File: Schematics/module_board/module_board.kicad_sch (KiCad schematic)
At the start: 38 parts, among them J1 Conn_01x01_Male, J2 Conn_01x06_Male, J3 Conn_01x06_Male, SW1 SW_SPST, SW2 SW_Push, SW3 SW_Push, SW4 SW_Push, SW5 SW_Push, SW6 SW_Push, U1 RP2040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

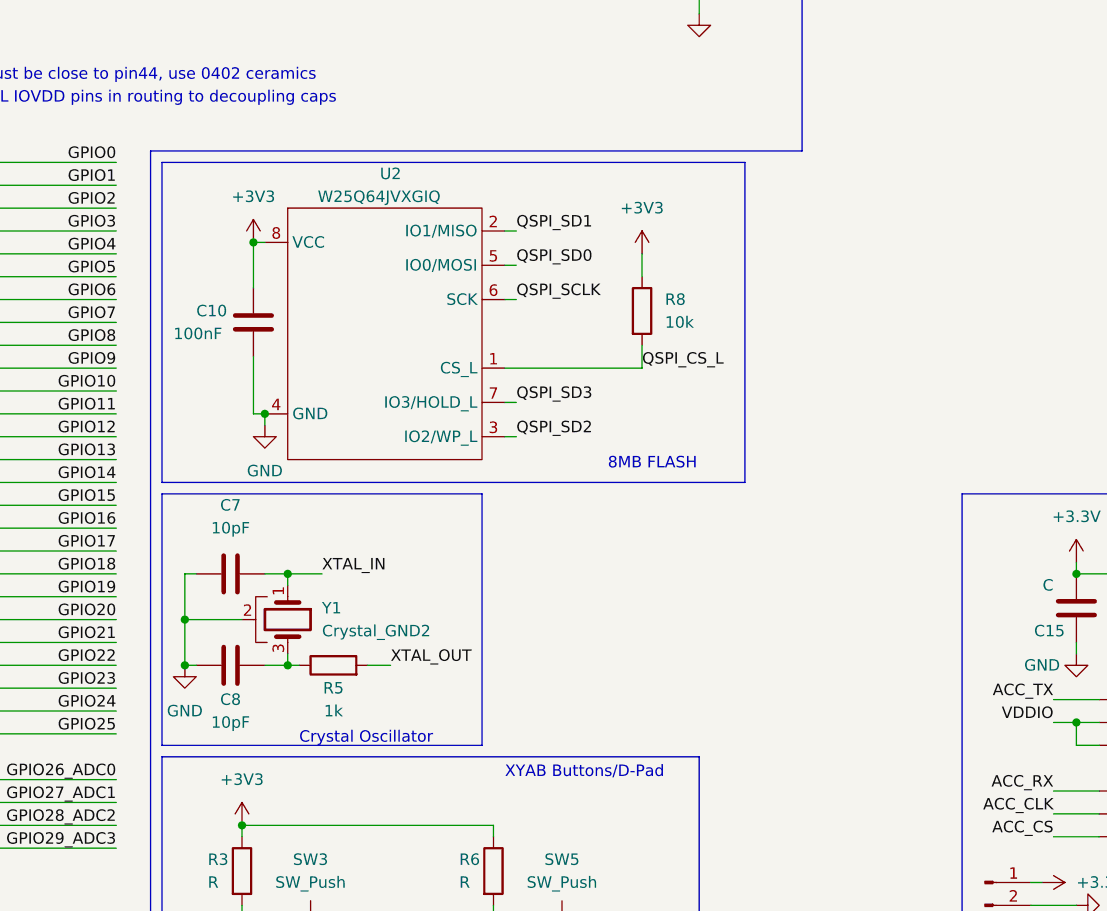
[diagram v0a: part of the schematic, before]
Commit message: updated crystal oscillator and flash memory on module board
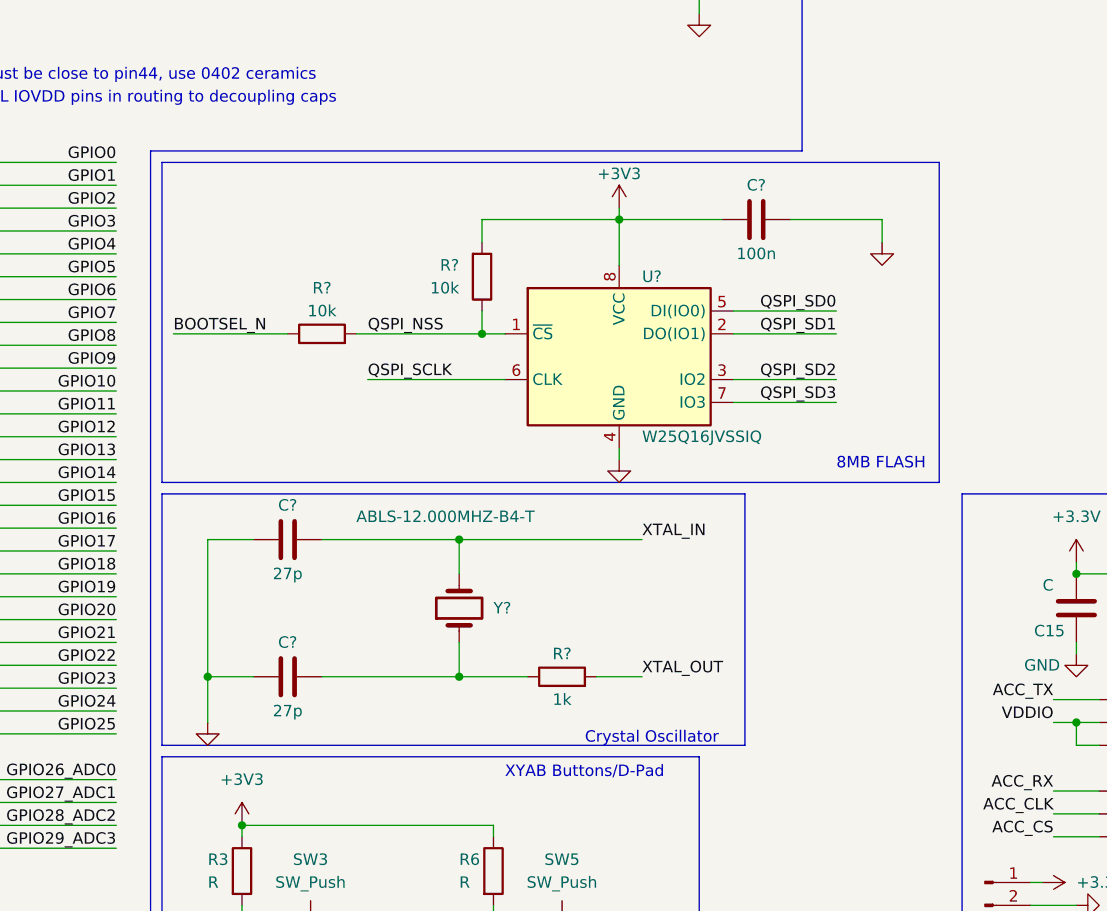
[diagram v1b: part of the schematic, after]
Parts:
- removed C10: 100nF, Capacitor_SMD:C_0402_1005Metric, symbol Device:C
- removed C7, C8: 10pF, Capacitor_SMD:C_0402_1005Metric, symbol Device:C
- removed R5: 1k, symbol Device:R
- removed R8: 10k, symbol Device:R
- removed U2: W25Q64JVXGIQ, symbol Flash_Memory:W25Q64JVXGIQ
- removed Y1: Crystal_GND2, symbol Device:Crystal_GND2
- added C? (x2): 27p, symbol Device:C
- added C?: 100n, symbol Device:C
- added R? (x2): 10k, symbol Device:R
- added R?: 1k, symbol Device:R
- added U?: W25Q16JVSSIQ, symbol Merrick_Symbols_KiCad6:W25Q16JVSSIQ
- added Y?: ABLS-12.000MHZ-B4-T, symbol Device:Crystal
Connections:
- net +3V3: now also C?.1, R?.2, U?.8 (VCC)
- net GND: now also C?.1, C?.1, C?.2, U?.4 (GND)
- net QSPI_NSS: now also R?.1, R?.2, U?.1 (~{CS})
- net QSPI_SCLK: now also U?.6 (CLK)
- net QSPI_SD0: now also U?.5 (DI(IO0))
- net QSPI_SD1: now also U?.2 (DO(IO1))
- net QSPI_SD2: now also U?.3 (IO2)
- net QSPI_SD3: now also U?.7 (IO3)
- net XTAL_IN: now also C?.2, Y?.2
- net XTAL_OUT: now also R?.2
- new net: C?.2, R?.1, Y?.1
- new net BOOTSEL_N: R?.1

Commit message: updated footprint for module board
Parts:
- C10, C7, C8: renamed from C?; footprint (none) -> Capacitor_SMD:C_0402_1005Metric
- C3, C4: footprint Capacitor_SMD:C_0603_1608Metric -> Capacitor_SMD:C_0402_1005Metric
- R5, R8, R9: renamed from R?; footprint (none) -> Resistor_SMD:R_0402_1005Metric
- U2: renamed from U?; footprint (none) -> W25Q16JVSSIQ:SOIC127P790X216-8N
- Y1: renamed from Y?; footprint (none) -> ABLS-12:XTAL_ABLS-12.000MHZ-B4-T

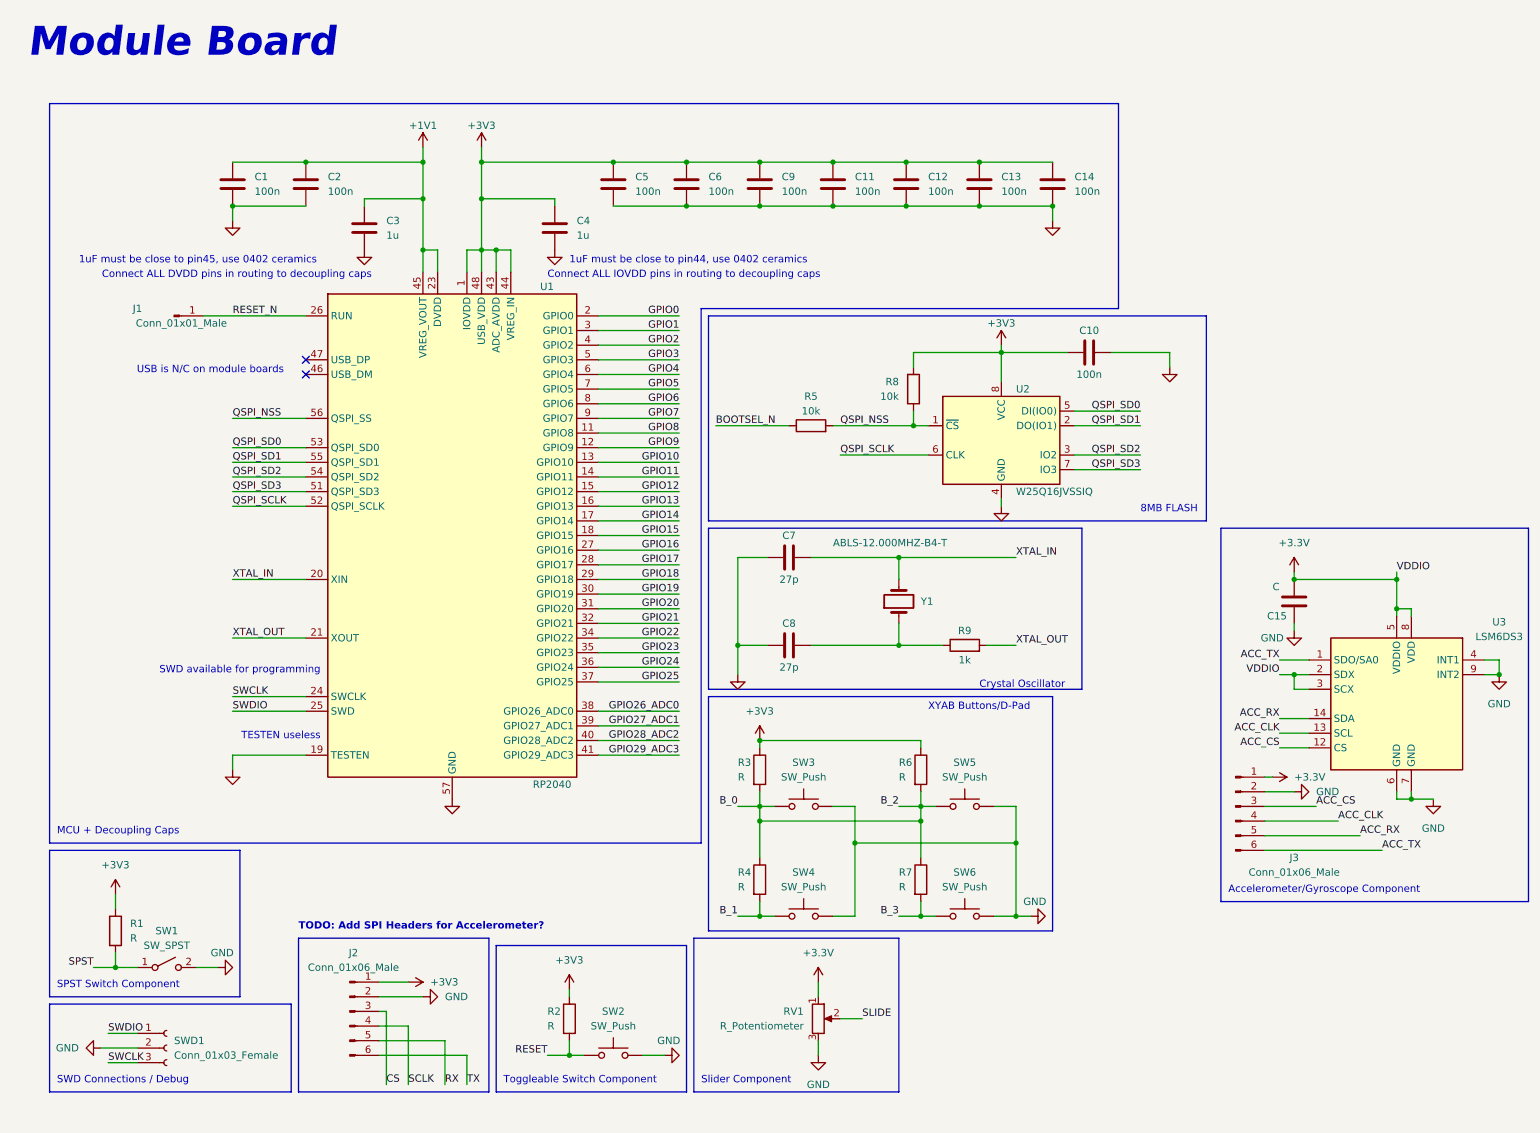
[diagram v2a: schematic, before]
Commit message: Separated Module Components
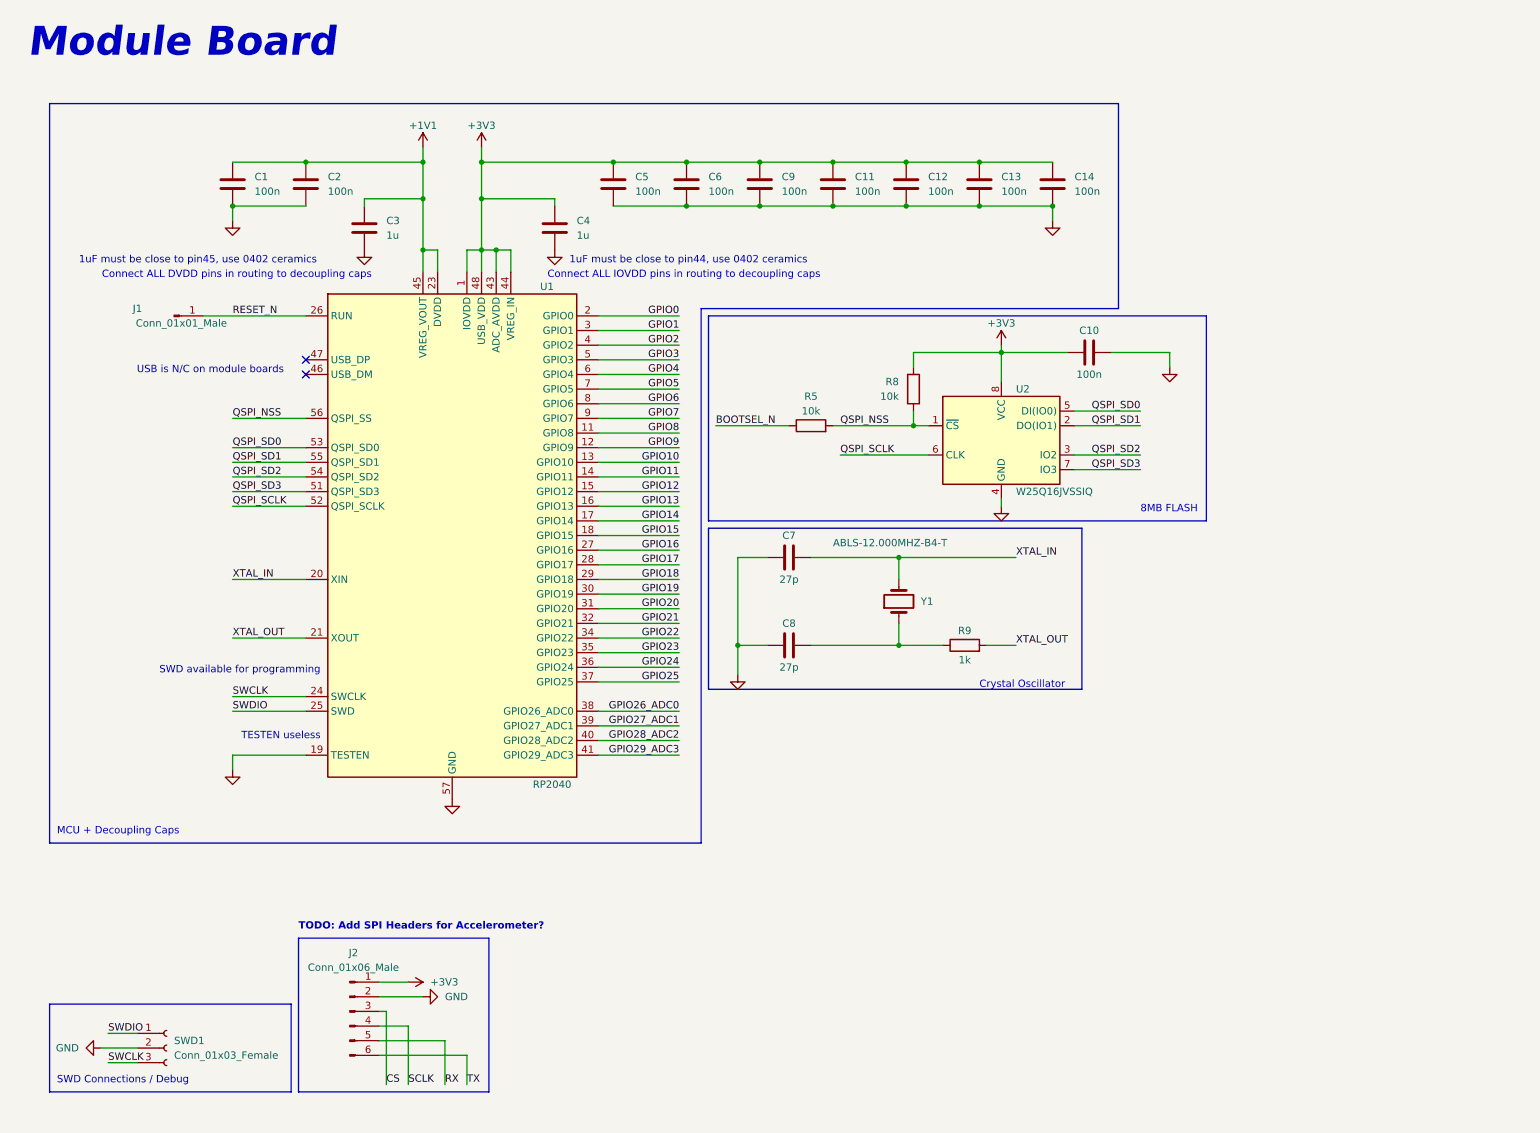
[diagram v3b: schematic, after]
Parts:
- removed C15: C, Capacitor_SMD:C_0402_1005Metric, symbol Device:C
- removed J3: Conn_01x06_Male, symbol Connector:Conn_01x06_Male
- removed R1, R2, R3, R4, R6, R7: R, symbol Device:R
- removed RV1: R_Potentiometer, symbol Device:R_Potentiometer
- removed SW1: SW_SPST, symbol Switch:SW_SPST
- removed SW2, SW3, SW4, SW5, SW6: SW_Push, symbol Switch:SW_Push
- removed U3: LSM6DS3, Package_LGA:LGA-14_3x2.5mm_P0.5mm_LayoutBorder3x4y, symbol Sensor_Motion:LSM6DS3
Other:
- note removed: "Accelerometer/Gyroscope Component"
- note removed: "SPST Switch Component"
- note removed: "Slider Component"
- note removed: "Toggleable Switch Component"
- note removed: "XYAB Buttons/D-Pad"

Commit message: Updated Footprints, started PCB design
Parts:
- removed J2: Conn_01x06_Male, symbol Connector:Conn_01x06_Male
- removed SWD1: Conn_01x03_Female, symbol Connector:Conn_01x03_Female
- added J10, J5, J6, J7, J8, J9: Conn_01x01_Male, TestPoint:TestPoint_Plated_Hole_D2.0mm, symbol Connector:Conn_01x01_Male
- added J2, J3, J4: Conn_01x01_Male, TestPoint:TestPoint_Pad_D2.0mm, symbol Connector:Conn_01x01_Male
- J1: footprint (none) -> TestPoint:TestPoint_Pad_D2.0mm
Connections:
- net +1V1: now also C3.2; no longer C3.1
- net +3V3: now also J5.1 (Pin_1)
- net CS: now also J7.1 (Pin_1)
- net GND: now also C3.1, J3.1 (Pin_1), J6.1 (Pin_1); no longer C3.2
- net RX: now also J9.1 (Pin_1)
- net SCLK: now also J8.1 (Pin_1)
- net SWCLK: now also J4.1 (Pin_1)
- net SWDIO: now also J2.1 (Pin_1)
- net TX: now also J10.1 (Pin_1)
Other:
- moved on the sheet: C3

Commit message: Modified flash footprint
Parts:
- U2: footprint W25Q16JVSSIQ:SOIC127P790X216-8N -> Package_SO:SOIC-8_5.23x5.23mm_P1.27mm
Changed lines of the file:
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@@
       (effects (font (size 1.27 1.27)) (justify left))
     )
-    (property "Footprint" "W25Q16JVSSIQ:SOIC127P790X216-8N" (id 2) (at 158.75 80.01 0)
+    (property "Footprint" "Package_SO:SOIC-8_5.23x5.23mm_P1.27mm" (id 2) (at 158.75 80.01 0)
       (effects (font (size 1.27 1.27)) hide)
     )
@@
     )
     (path "/216ca7a2-00a8-4a6f-813d-3ef99867e82d"
-      (reference "U2") (unit 1) (value "W25Q16JVSSIQ") (footprint "W25Q16JVSSIQ:SOIC127P790X216-8N")
+      (reference "U2") (unit 1) (value "W25Q16JVSSIQ") (footprint "Package_SO:SOIC-8_5.23x5.23mm_P1.27mm")
     )
     (path "/039132b5-d1ff-4807-8a71-1bea6b495b8f"
